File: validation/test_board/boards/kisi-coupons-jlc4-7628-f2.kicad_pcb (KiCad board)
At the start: 4 copper layers, 35 x 96 mm, 16 parts, among them J1 292-J-P-EP-ST-EL-01, J10 292-J-P-EP-ST-EL-01, J11 292-J-P-EP-ST-EL-01, J12 292-J-P-EP-ST-EL-01, J13 292-J-P-EP-ST-EL-01, J14 292-J-P-EP-ST-EL-01, J15 292-J-P-EP-ST-EL-01, J16 292-J-P-EP-ST-EL-01, J2 292-J-P-EP-ST-EL-01, J3 292-J-P-EP-ST-EL-01, J4 292-J-P-EP-ST-EL-01, J5 292-J-P-EP-ST-EL-01, J6 292-J-P-EP-ST-EL-01, J7 292-J-P-EP-ST-EL-01, J8 292-J-P-EP-ST-EL-01, J9 292-J-P-EP-ST-EL-01

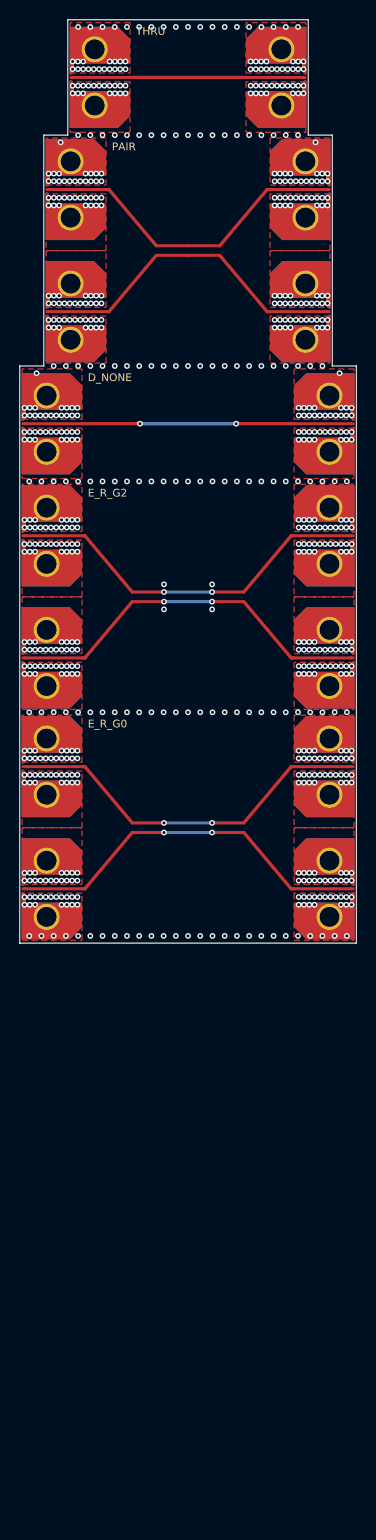
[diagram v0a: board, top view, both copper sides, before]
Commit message: First order: two 4-layer boards and one 6-layer board
- Maintainer's layout (2026-10-31): jlc4-7628-f1 100 x 96 mm (THRU,
  CPWG L / 2L, XT_MS, G_CAV), jlc4-7628-f2 35 x 156 mm (THRU, A x 3,
  D 0.7 / 2 mm / none, PAIR, E with 2 and 0 GND vias), jlc6-7628-f1
  50 x 132 mm (THRU, SL_L3 / VLV_L3, B_L1L6, PAIR, E_R_G2, D x 3). One
  2x-thru per board. An edge launch needs 12 mm of edge per connector
  and side, so the 4-layer set cannot share one 100 x 100 mm board; the
  two boards above their price bracket get their own size limits.
- DRC (KiCad 7, converted copies): no errors; kisi check rerun; the
  first-order table in test_board.md and README lists the exact sizes.

Co-Authored-By: Claude Opus 5.5 <noreply@anthropic.com>
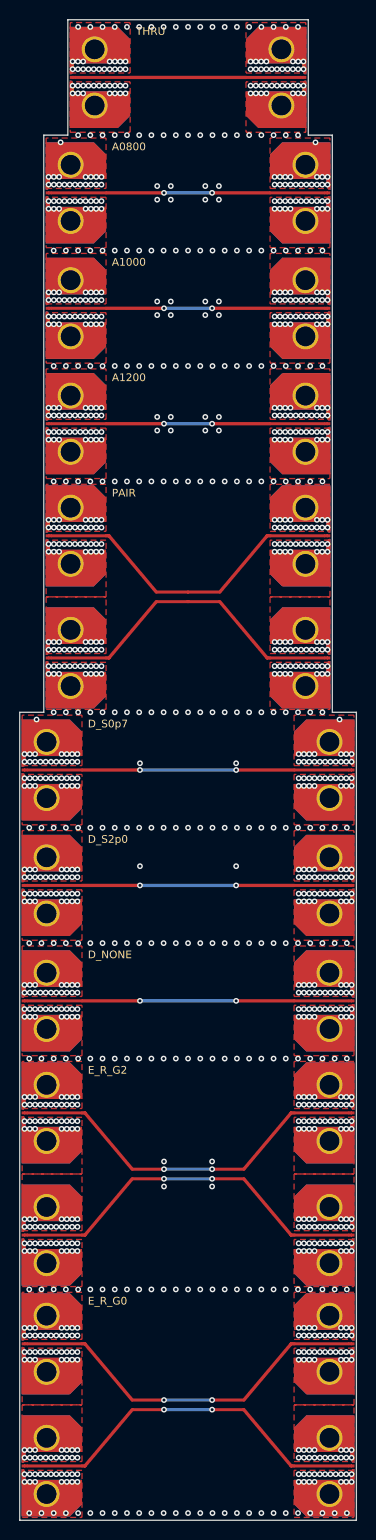
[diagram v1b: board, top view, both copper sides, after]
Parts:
- added J17: 292-J-P-EP-ST-EL-01, kisi_coupons:Samtec_292-J-P-EP-ST-EL-01_EdgeLaunch, F.Cu at (30.0, 132.0)
- added J18: 292-J-P-EP-ST-EL-01, kisi_coupons:Samtec_292-J-P-EP-ST-EL-01_EdgeLaunch, F.Cu at (65.0, 132.0)
- added J19: 292-J-P-EP-ST-EL-01, kisi_coupons:Samtec_292-J-P-EP-ST-EL-01_EdgeLaunch, F.Cu at (30.0, 143.7)
- added J20: 292-J-P-EP-ST-EL-01, kisi_coupons:Samtec_292-J-P-EP-ST-EL-01_EdgeLaunch, F.Cu at (30.0, 156.3)
- added J21: 292-J-P-EP-ST-EL-01, kisi_coupons:Samtec_292-J-P-EP-ST-EL-01_EdgeLaunch, F.Cu at (65.0, 143.7)
- added J22: 292-J-P-EP-ST-EL-01, kisi_coupons:Samtec_292-J-P-EP-ST-EL-01_EdgeLaunch, F.Cu at (65.0, 156.3)
- added J23: 292-J-P-EP-ST-EL-01, kisi_coupons:Samtec_292-J-P-EP-ST-EL-01_EdgeLaunch, F.Cu at (30.0, 167.7)
- added J24: 292-J-P-EP-ST-EL-01, kisi_coupons:Samtec_292-J-P-EP-ST-EL-01_EdgeLaunch, F.Cu at (30.0, 180.3)
- added J25: 292-J-P-EP-ST-EL-01, kisi_coupons:Samtec_292-J-P-EP-ST-EL-01_EdgeLaunch, F.Cu at (65.0, 167.7)
- added J26: 292-J-P-EP-ST-EL-01, kisi_coupons:Samtec_292-J-P-EP-ST-EL-01_EdgeLaunch, F.Cu at (65.0, 180.3)
- moved J14 37.1 mm to (65.0, 108.0), turned to 180 degrees
- moved J15 37.1 mm to (30.0, 120.0), turned to 0 degrees
- moved J4 32.4 mm to (62.5, 48.0), turned to 180 degrees
- moved J5 32.4 mm to (32.5, 60.0), turned to 0 degrees
- moved J10 2.50 mm to (32.5, 96.3)
- moved J11 2.50 mm to (62.5, 83.7)
- moved J12 2.50 mm to (62.5, 96.3)
- moved J7 2.50 mm to (32.5, 72.0)
- moved J8 2.50 mm to (62.5, 72.0)
- moved J9 2.50 mm to (32.5, 83.7)
- moved J3 0.35 mm to (32.5, 48.0)
- moved J6 0.35 mm to (62.5, 60.0)
- moved J13 0.35 mm to (30.0, 108.0)
- moved J16 0.35 mm to (65.0, 120.0)
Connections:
- net SE_D_NONE renamed SE_A1200
- J10 pad 1: DP_E_R_G2_N -> DP_PAIR_N
- J11 pad 1: DP_E_R_G2_P -> DP_PAIR_P
- J12 pad 1: DP_E_R_G2_N -> DP_PAIR_N
- J13 pad 1: DP_E_R_G0_P -> SE_D_S0p7
- J14 pad 1: DP_E_R_G0_N -> SE_D_S0p7
- J15 pad 1: DP_E_R_G0_P -> SE_D_S2p0
- J16 pad 1: DP_E_R_G0_N -> SE_D_S2p0
- J3 pad 1: DP_PAIR_P -> SE_A0800
- J4 pad 1: DP_PAIR_N -> SE_A0800
- J5 pad 1: DP_PAIR_P -> SE_A1000
- J6 pad 1: DP_PAIR_N -> SE_A1000
- J9 pad 1: DP_E_R_G2_P -> DP_PAIR_P
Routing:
- net SE_D_S2p0: track 0.00 -> 33.4 mm, vias 0 -> 2
- net SE_D_S0p7: track 0.00 -> 33.4 mm, vias 0 -> 2
- net SE_D_NONE: track 0.00 -> 33.4 mm, vias 0 -> 2
- net SE_A1000: track 0.00 -> 28.4 mm, vias 0 -> 2
- net SE_A0800: track 0.00 -> 28.4 mm, vias 0 -> 2
- net SE_A1200: track 33.4 -> 28.4 mm
- net GND: vias 726 -> 1237
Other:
- board size 35 x 96 mm -> 35 x 156 mm
- board text added: "2026-10-31"
- board text added: "A0800"
- board text added: "A1000"
- board text added: "A1200"
- board text added: "D_S0p7"
- board text added: "D_S2p0"
- board text added: "kisi-coupons-jlc4-7628-f2: kisi measurement coupons v3 (2026-10-31)"
- board text removed: "2026-10-30"
- board text removed: "kisi-coupons-jlc4-7628-f2: kisi measurement coupons v3 (2026-10-30)"

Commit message: Coupon boards: own zone priorities, project-local footprint library
- KiCad 8/9 DRC reported overlapping zones of equal priority (the GND
  pour rectangles on L1 meet at 4-port launch pairs and along the CPWG
  coupons: 78 pairs on 26 boards). Every zone now has its own priority
  (planes 0, pours 1, 2, ..., islands and patches above); an outline
  check finds no equal-priority overlap left.
- The footprints the boards use are written as a project-local library
  (boards/kisi_coupons.pretty + fp-lib-table with ${KIPRJMOD}): the
  Samtec launch per launch width, the capacitor land patterns, the IC
  pin fields; per-instance Port/Status fields dropped, so board and
  library match. DRC (KiCad 7 on converted copies, with the library):
  no library warnings, no errors; the first-order boards are clean.
- Boards regenerated, kisi check unchanged.

Co-Authored-By: Claude Opus 5.5 <noreply@anthropic.com>
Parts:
- removed the J17 at (30.0, 132.0)
- removed the J25 at (65.0, 167.7)
- removed the J9 at (32.5, 83.7)
- added J15: 292-J-P-EP-ST-EL-01, kisi_coupons:Samtec_292-J-P-EP-ST-EL-01_EdgeLaunch_W0.315, F.Cu at (30.0, 120.0)
- added J22: 292-J-P-EP-ST-EL-01, kisi_coupons:Samtec_292-J-P-EP-ST-EL-01_EdgeLaunch_W0.315, F.Cu at (65.0, 156.3)
- added J8: 292-J-P-EP-ST-EL-01, kisi_coupons:Samtec_292-J-P-EP-ST-EL-01_EdgeLaunch_W0.315, F.Cu at (62.5, 72.0)
- J1, J10, J11, J12, J13, J14, J16, J18, J19, J2, J20, J21, J23, J24, J26, J3, J4, J5, J6, J7: footprint kisi_coupons:Samtec_292-J-P-EP-ST-EL-01_EdgeLaunch -> kisi_coupons:Samtec_292-J-P-EP-ST-EL-01_EdgeLaunch_W0.315
- J17: renamed from J15; footprint kisi_coupons:Samtec_292-J-P-EP-ST-EL-01_EdgeLaunch -> kisi_coupons:Samtec_292-J-P-EP-ST-EL-01_EdgeLaunch_W0.315
- J25: renamed from J22; footprint kisi_coupons:Samtec_292-J-P-EP-ST-EL-01_EdgeLaunch -> kisi_coupons:Samtec_292-J-P-EP-ST-EL-01_EdgeLaunch_W0.315
- J9: renamed from J8; footprint kisi_coupons:Samtec_292-J-P-EP-ST-EL-01_EdgeLaunch -> kisi_coupons:Samtec_292-J-P-EP-ST-EL-01_EdgeLaunch_W0.315
- moved J9 32.2 mm to (32.5, 83.7), turned to 0 degrees
- moved J17 12.0 mm to (30.0, 132.0)
- moved J25 11.3 mm to (65.0, 167.7)
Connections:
- J17 pad 1: SE_D_S2p0 -> SE_D_NONE
- J25 pad 1: DP_E_R_G2_N -> DP_E_R_G0_P
- J9 pad 1: SE_A1200 -> DP_PAIR_P
